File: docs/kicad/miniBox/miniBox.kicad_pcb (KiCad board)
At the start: 2 copper layers, 53 x 41 mm, 19 parts, among them J1 FAN, J2 CONTROLLER, J3 INV_CONN, J4 INV_PWR, Q1 BC557 PNP, SW1 OVERRIDE, SW2 LOW/HIGH

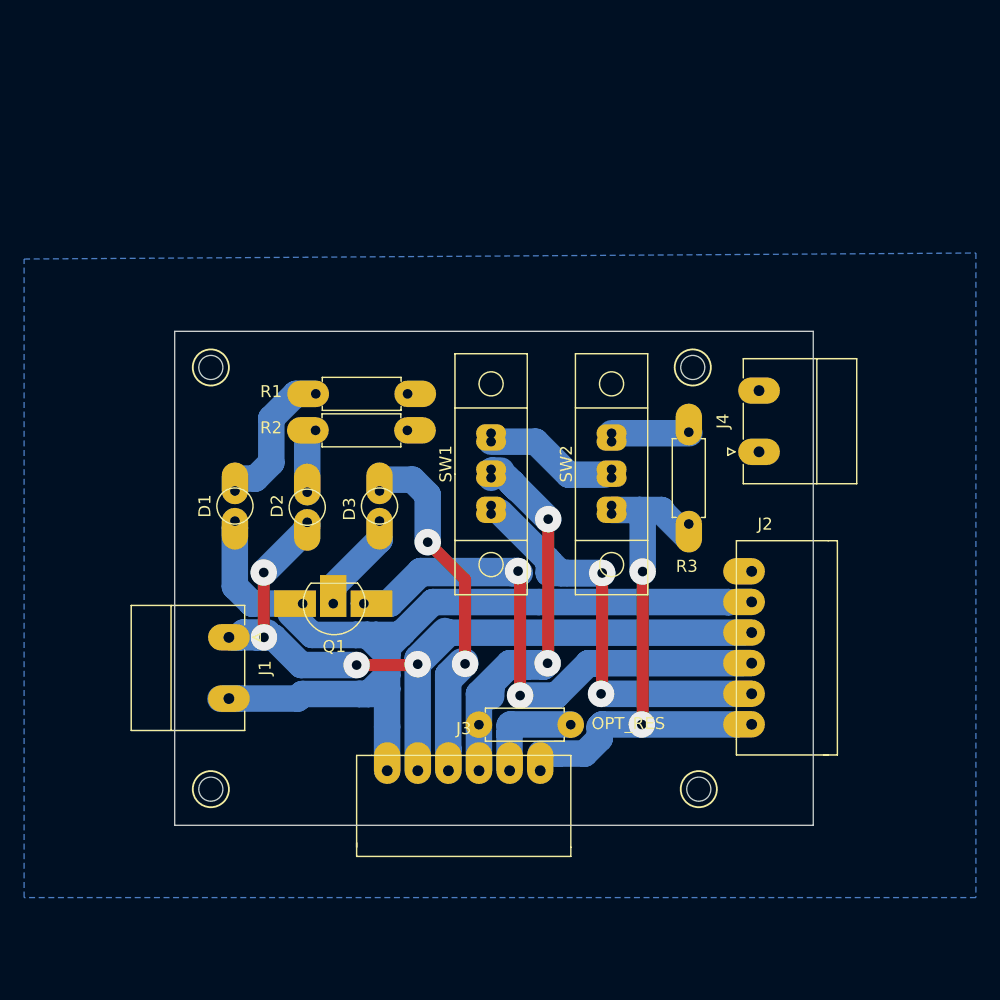
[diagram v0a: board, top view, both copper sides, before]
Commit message: produced fridgeController pcb's "board1" and "miniBox"
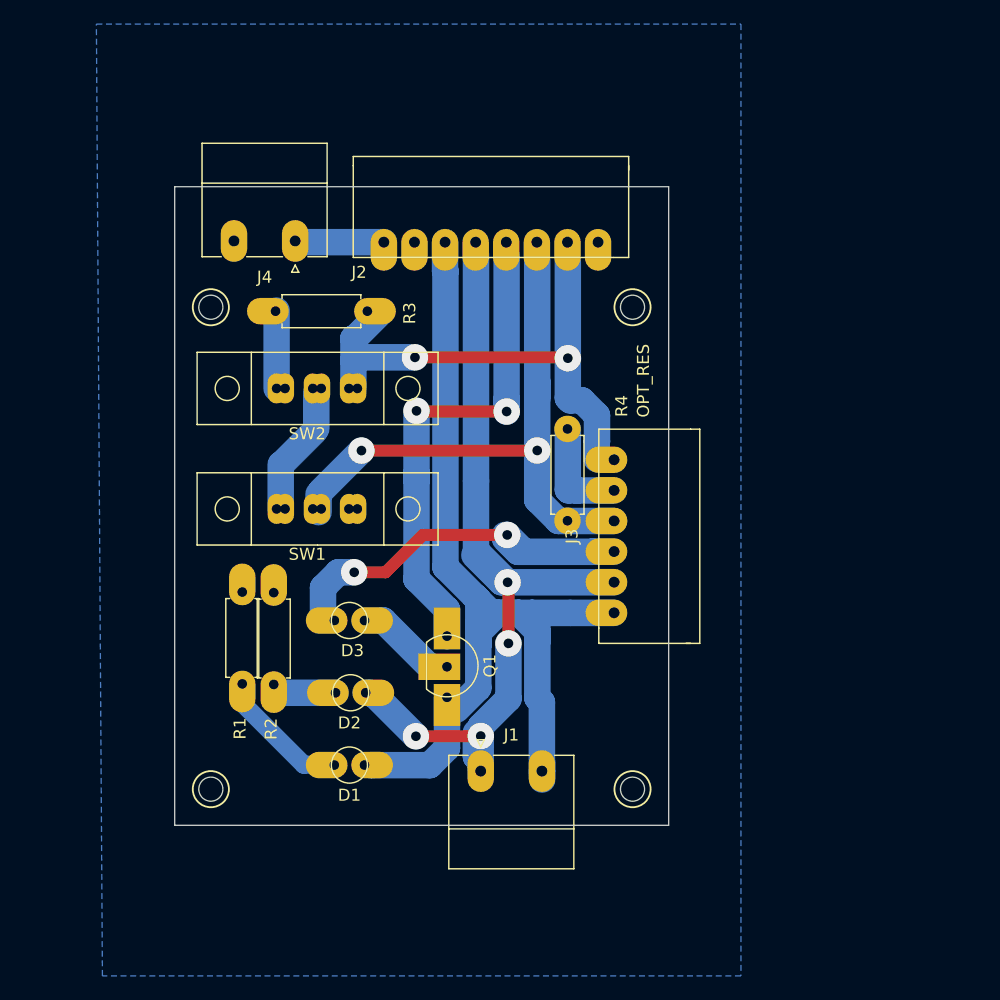
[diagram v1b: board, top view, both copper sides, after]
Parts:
- removed OPT_RES: myResistor, 0_my_footprints:myResistor
- removed the REF** at (105.0, 57.5)
- removed the REF** at (65.0, 57.5)
- added R4: 10K?, 0_my_footprints2:resistor, F.Cu at (94.6, 62.6)
- added REF**: myMountingHole_2.0mm, 0_my_footprints:myMountingHole_2.0mm, F.Cu at (65.0, 52.5)
- added REF**: myMountingHole_2.0mm, 0_my_footprints:myMountingHole_2.0mm, F.Cu at (65.0, 92.5)
- J2: footprint 0_my_footprints2:myJST6_right -> 0_my_footprints2:myJST8_right
- moved J4 42.3 mm to (72.0, 47.0), turned to 180 degrees
- moved J2 42.0 mm to (97.1, 47.1), turned to 180 degrees
- moved REF** 40.4 mm to (100.0, 52.5), turned to 90 degrees
- moved REF** 35.0 mm to (100.0, 92.5), turned to 90 degrees
- moved R3 32.0 mm to (78.0, 52.8), turned to 180 degrees
- moved SW2 25.4 mm to (73.9, 59.2), turned to 180 degrees
- moved J1 23.7 mm to (87.4, 91.0), turned to 0 degrees
- moved D1 23.5 mm to (76.5, 90.5), turned to 0 degrees
- moved J3 22.9 mm to (98.5, 77.9), turned to 90 degrees
- moved R1 21.4 mm to (67.6, 76.1), turned to 270 degrees
- moved R2 17.4 mm to (70.2, 76.2), turned to 270 degrees
- moved D2 15.8 mm to (76.6, 84.5), turned to 0 degrees
- moved SW1 14.7 mm to (73.9, 69.2), turned to 180 degrees
- moved D3 9.82 mm to (76.5, 78.5), turned to 0 degrees
- moved Q1 7.41 mm to (84.6, 79.8), turned to 270 degrees
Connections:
- J2 pad 1: T -> GND
- J2 pad 2: C2 -> T
- J2 pad 3: DIAG_DIODE -> C
- J2 pad 4: FAN- -> DIAG_DIODE
- J2 pad 5: FAN_DIODE+ -> FAN-
- J2 pad 6: GND -> FAN_DIODE+
- J4 pad 1: Net-(J4-Pad1) -> +12V
- SW1 pad 1: C2 -> Net-(SW1-Pad1)
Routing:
- net C2: track 37.8 -> 0.00 mm, vias 2 -> 0
- net DIAG_DIODE: track 59.6 -> 43.1 mm
- net (no net): track 8.84 -> 0.00 mm
- net P: track 0.00 -> 8.84 mm
- net C: track 40.4 -> 49.1 mm
- net +12V: track 0.00 -> 7.36 mm
- net FAN_DIODE+: track 86.1 -> 88.5 mm
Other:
- board size 53 x 41 mm -> 41 x 53 mm
- board text added: "OPT_RES"

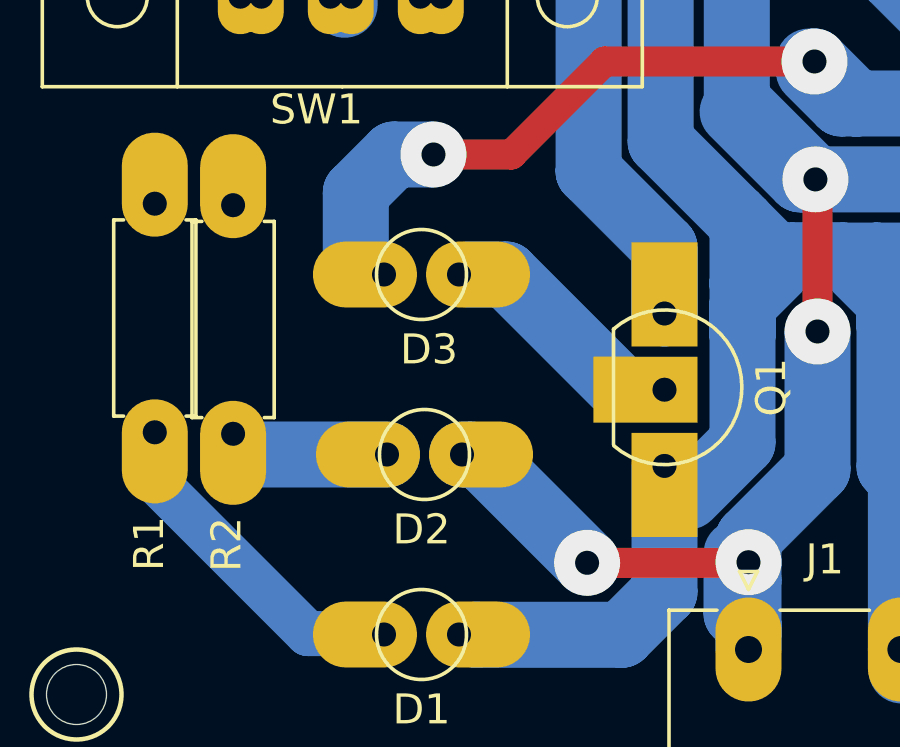
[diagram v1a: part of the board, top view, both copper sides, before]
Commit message: kicad - miniBox - corrected routing of FAN DIODE from FAN- to FAN/DIODE+ instead of GND
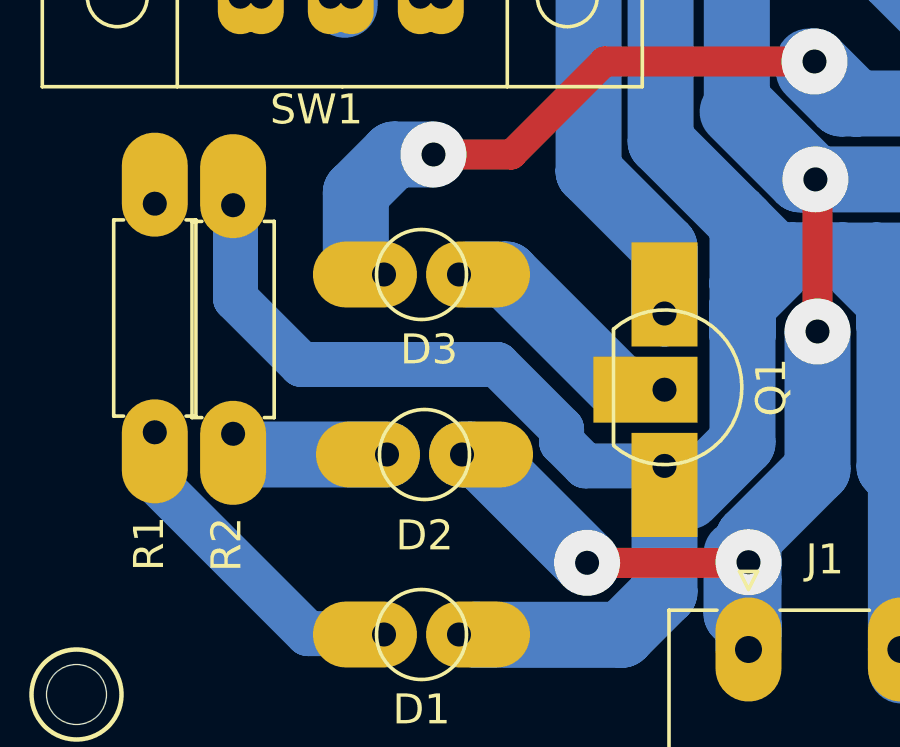
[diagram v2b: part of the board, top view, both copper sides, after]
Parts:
- R2: value 1.2K -> 1.5K
- turned D2 to 180 degrees
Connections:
- D2 pad 1: Net-(D2-Pad1) -> FAN-
- D2 pad 2: FAN- -> Net-(D2-Pad2)
- R2 pad 1: GND -> FAN_DIODE+
- R2 pad 2: Net-(D2-Pad1) -> Net-(D2-Pad2)
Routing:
- net FAN_DIODE+: track 88.5 -> 108.6 mm
- net Net-(D2-Pad2): track 0.00 -> 4.76 mm
- net Net-(D2-Pad1): track 4.76 -> 0.00 mm
